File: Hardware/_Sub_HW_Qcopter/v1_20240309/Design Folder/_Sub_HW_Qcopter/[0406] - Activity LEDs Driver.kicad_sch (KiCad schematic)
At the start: 0 parts

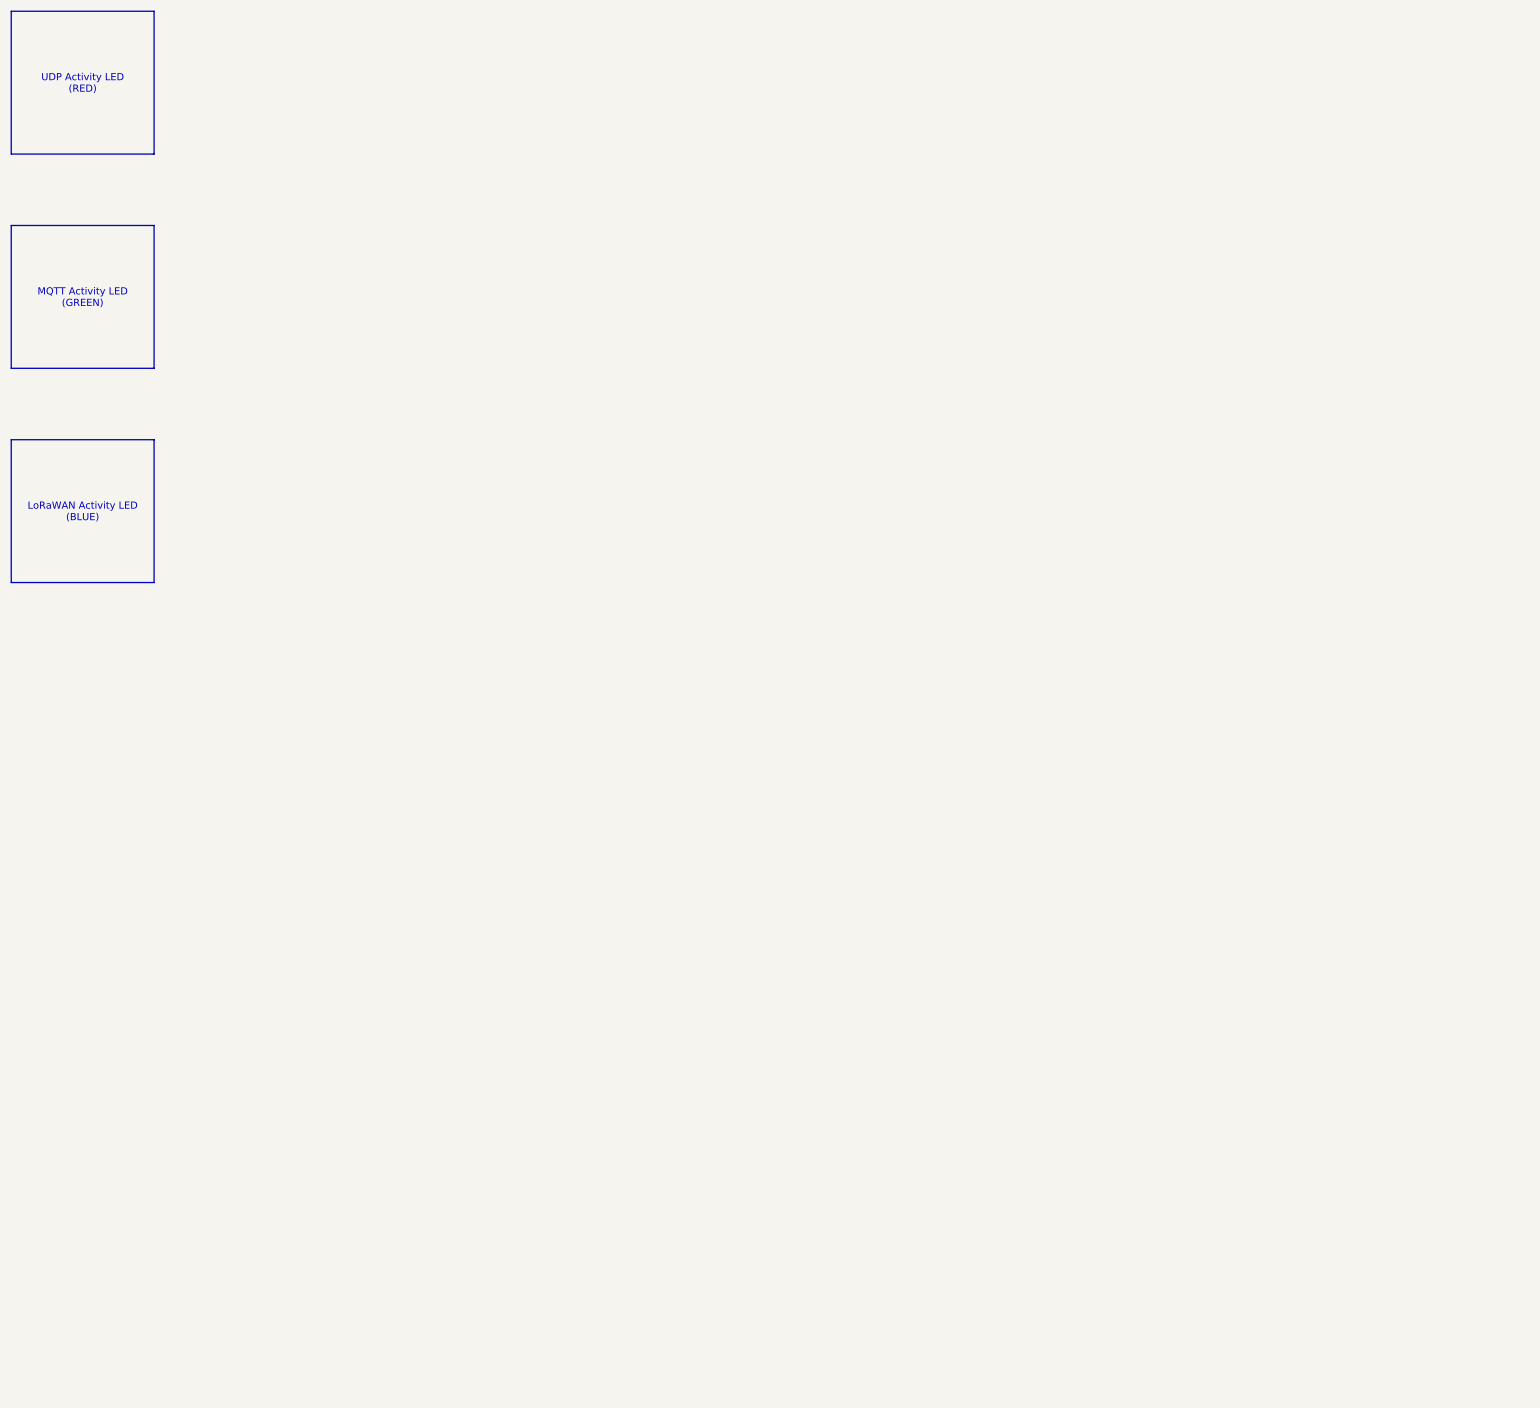
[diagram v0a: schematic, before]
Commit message: Schematic is done by 90%
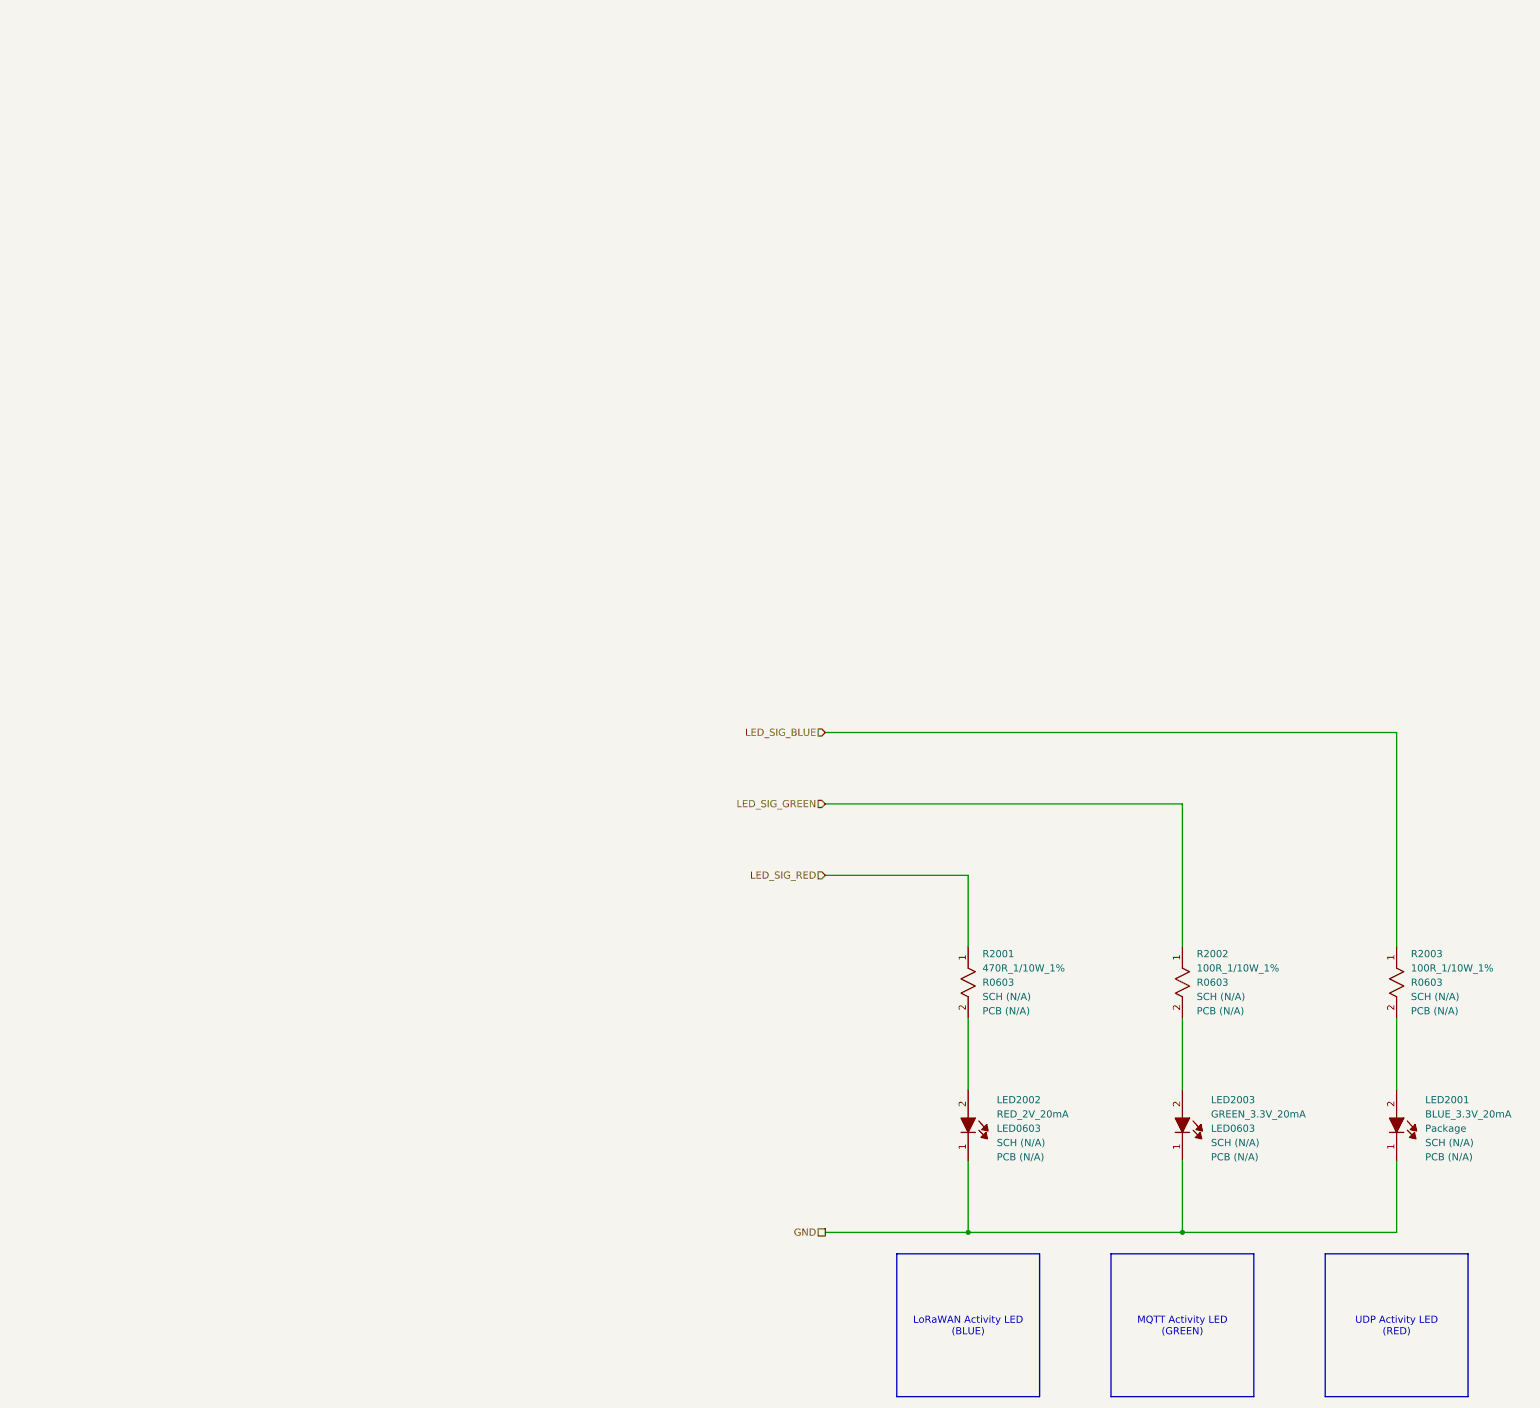
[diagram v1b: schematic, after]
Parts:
- added LED2001: BLUE_3.3V_20mA, LED_SMD:LED_0603_1608Metric, symbol _SCHLIB_Qcopter:DIODE_LED_BLUE_3.3V_20mA_470nm_LED0603
- added LED2002: RED_2V_20mA, LED_SMD:LED_0603_1608Metric, symbol _SCHLIB_Qcopter:DIODE_LED_RED_2V_20mA_624nm_LED0603
- added LED2003: GREEN_3.3V_20mA, LED_SMD:LED_0603_1608Metric, symbol _SCHLIB_Qcopter:DIODE_LED_GREEN_3.3V_20mA_525nm_LED0603
- added R2001: 470R_1/10W_1%, Resistor_SMD:R_0603_1608Metric, symbol _SCHLIB_Qcopter:RES_470R_1/10W_1%_R0603
- added R2002, R2003: 100R_1/10W_1%, Resistor_SMD:R_0603_1608Metric, symbol _SCHLIB_Qcopter:RES_100R_1/10W_1%_R0603
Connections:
- new net: LED2001.2, R2003.2
- new net: LED2003.2, R2002.2
- new net: LED2002.2, R2001.2
- new net GND: LED2001.1, LED2002.1, LED2003.1
- new net LED_SIG_BLUE: R2003.1
- new net LED_SIG_GREEN: R2002.1
- new net LED_SIG_RED: R2001.1
